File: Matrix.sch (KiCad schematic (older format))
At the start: 105 parts

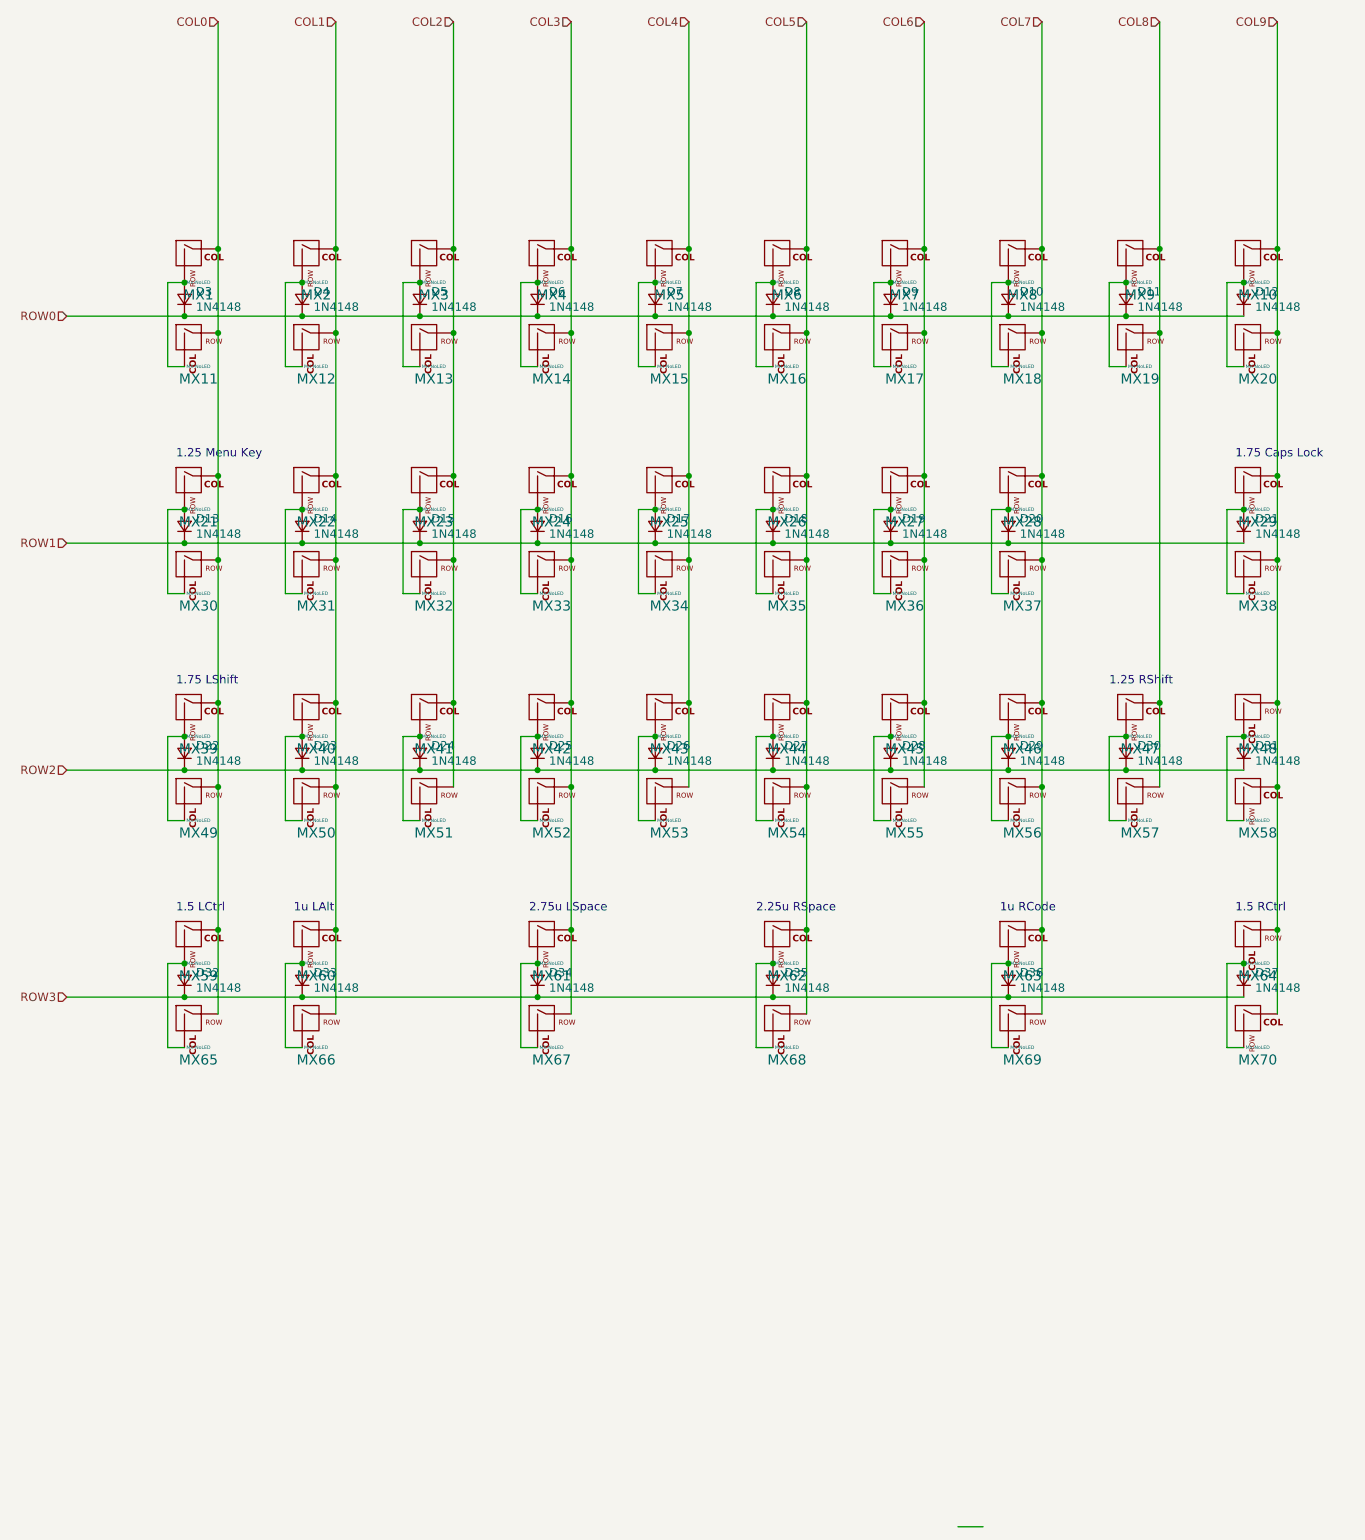
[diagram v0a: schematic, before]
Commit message: Add LCSC part numbers in BOM, fix RGB
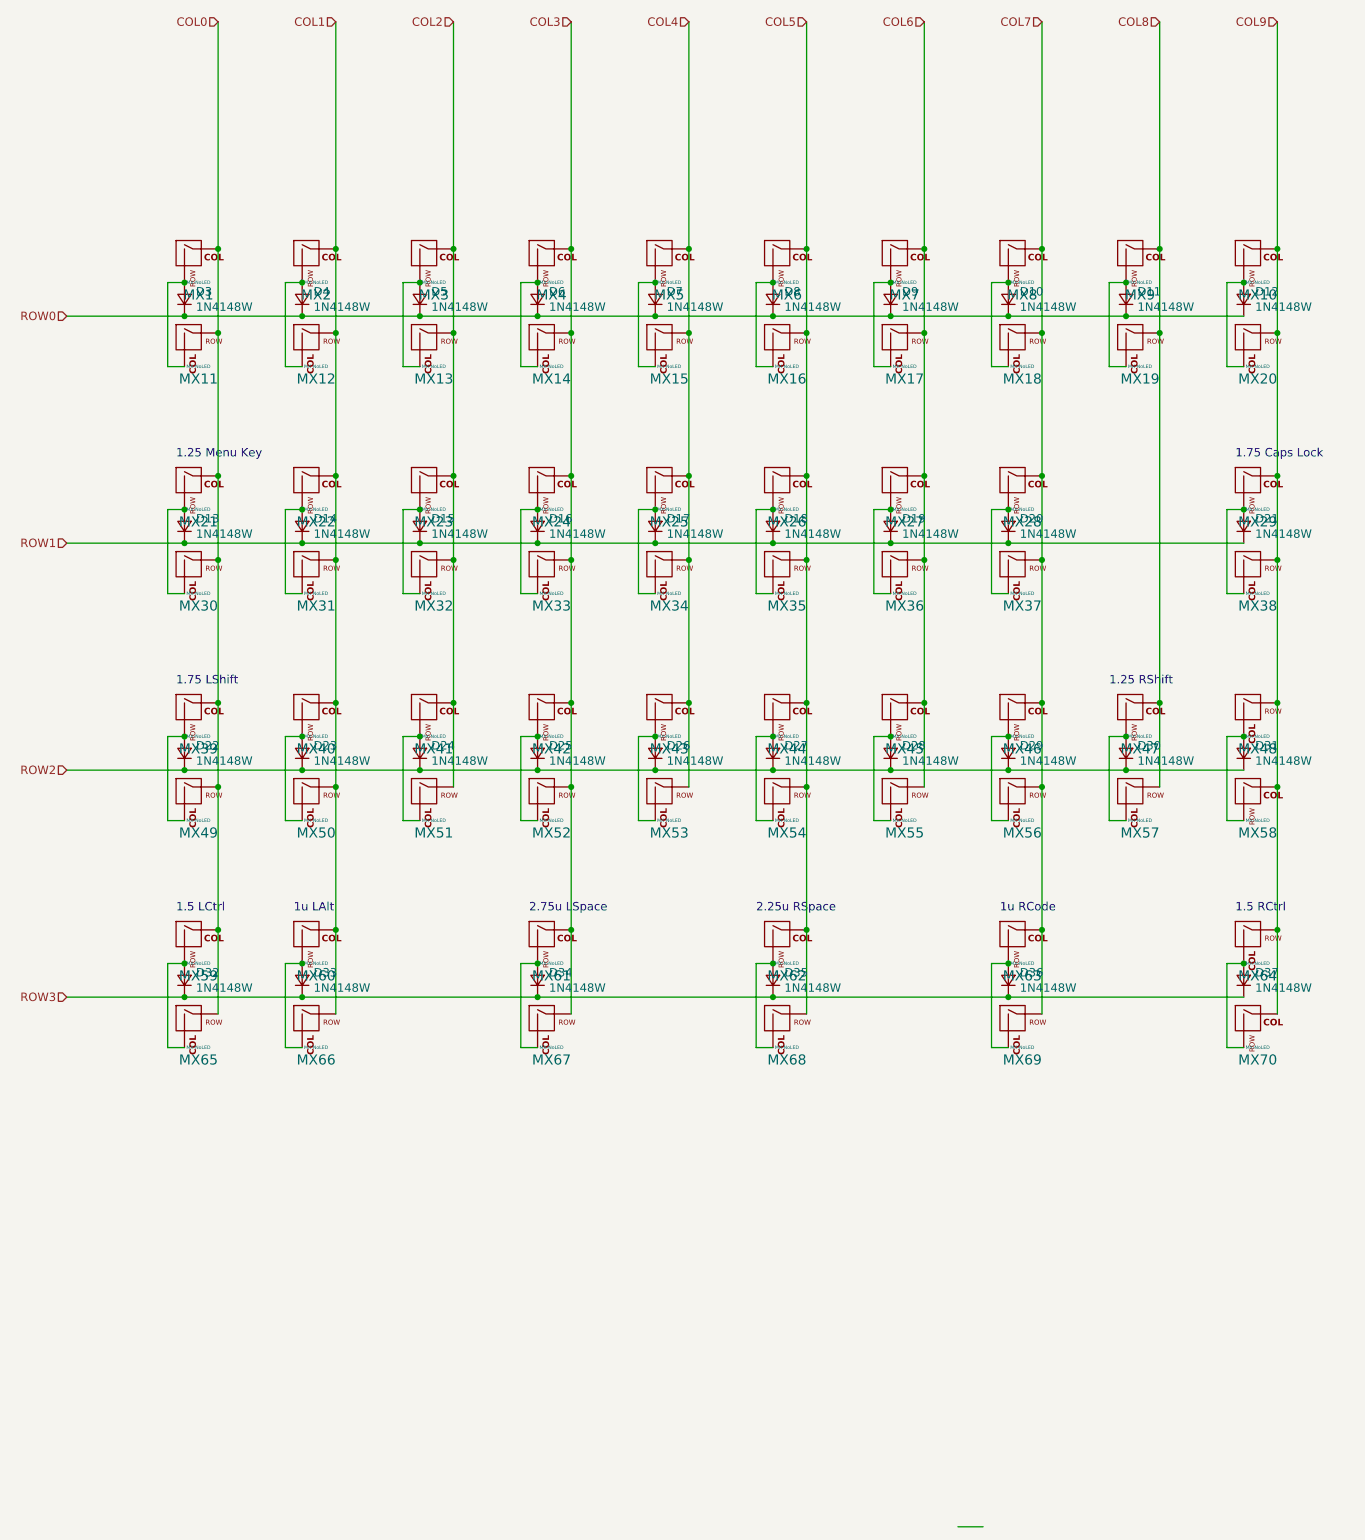
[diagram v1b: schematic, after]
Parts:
- D10, D11, D12, D13, D14, D15, D16, D17, D18, D19, D20, D21, D22, D23, D24, D25, D26, D27, D28, D29, D3, D30, D31, D32, D33, D34, D35, D36, D37, D4, D5, D6, D7, D8, D9: value 1N4148 -> 1N4148W; LCSC (none) -> C81598
